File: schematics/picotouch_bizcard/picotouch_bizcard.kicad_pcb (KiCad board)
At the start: 2 copper layers, 88.9 x 50.8 mm, 48 parts, among them J2 AudioJack4, SW1 Capacitive Button, SW10 Capacitive Button, SW11 Capacitive Button, SW12 Capacitive Button, SW2 Capacitive Button, SW3 Capacitive Button, SW4 Capacitive Button, SW5 Capacitive Button, SW6 Capacitive Button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

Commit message: silkscreen
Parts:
- moved R16 1.02 mm to (132.1, 71.1)
- moved D6 0.89 mm to (127.0, 71.1)
- moved U1 0.51 mm to (127.8, 50.8)
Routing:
- net +3.3V: track 115.2 -> 114.1 mm
- net /TOUCH11: track 62.5 -> 63.2 mm
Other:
- board text added: "0"
- board text added: "1"
- board text added: "2"
- board text added: "3"
- board text added: "4"
- board text added: "5"
- board text added: "6"
- board text added: "7"
- board text added: "8"
- board text added: "<>"
- board text added: "@todbot"
- board text added: "MIDI OUT TRS-A"
- board text added: "X"
- board text added: "picotouch_bizcard 5 Jun 2024 - @todbot / Tod Kurt github.com/todbot/picotouch_bizcard"
- board text added: "picotouch_bizcard USB/MIDI controller"

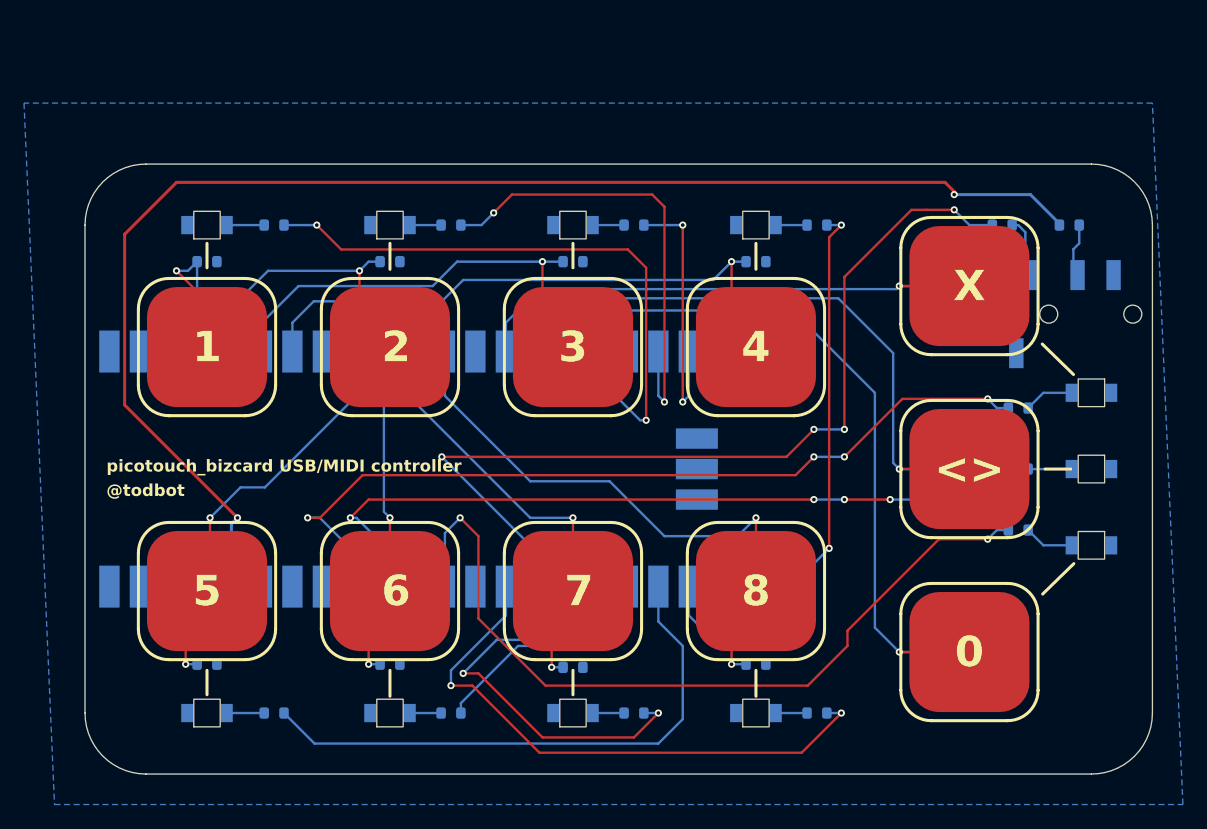
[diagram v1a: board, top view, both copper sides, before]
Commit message: added tx/rx test points and mounting hole
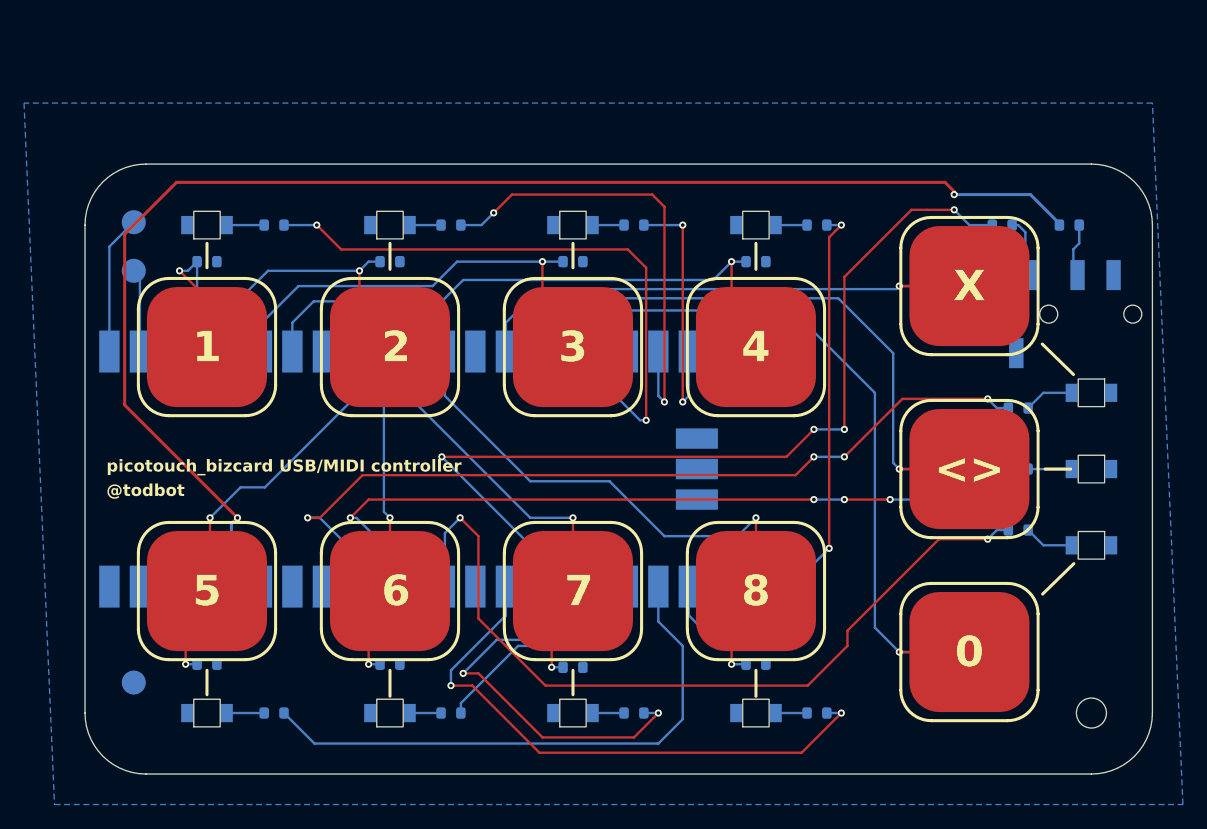
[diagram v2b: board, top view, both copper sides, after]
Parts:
- added H1: MountingHole, MountingHole:MountingHole_2.5mm, F.Cu at (185.4, 71.1)
- added TP1: TX, TestPoint:TestPoint_Pad_D2.0mm, B.Cu at (105.7, 30.2)
- added TP2: RX, TestPoint:TestPoint_Pad_D2.0mm, B.Cu at (105.7, 34.3)
- added TP3: GND, TestPoint:TestPoint_Pad_D2.0mm, B.Cu at (105.7, 68.6)
- SW1: footprint todbot_stuff:Pad-CapacitiveTouch-SparkFun -> SparkFun-Switch:Pad-CapacitiveTouch
- renumbered J2 to J1
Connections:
- U1 pad 1: unconnected-(U1-GPIO0-Pad1) -> /TX
- U1 pad 2: unconnected-(U1-GPIO1-Pad2) -> /RX
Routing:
- net /TX: track 0.00 -> 12.5 mm
- net /RX: track 0.00 -> 7.83 mm
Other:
- board text added: "gnd"
- board text added: "tx rx"

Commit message: submit to fab
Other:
- board text added: "JLCJLCJLCJLC"
- board text added: "picotouch_bizcard USB/MIDI controller / @todbot"
- board text removed: "@todbot"
- board text removed: "picotouch_bizcard USB/MIDI controller"
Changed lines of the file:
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@@
 		(sheetname "Root")
 		(sheetfile "picotouch_bizcard.kicad_sch")
-		(attr exclude_from_pos_files)
+		(attr exclude_from_pos_files exclude_from_bom)
 		(fp_circle
 			(center 0 0)
@@
 		(sheetname "Root")
 		(sheetfile "picotouch_bizcard.kicad_sch")
-		(attr exclude_from_pos_files)
+		(attr exclude_from_pos_files exclude_from_bom)
 		(fp_circle
 			(center 0 0)
@@
 		(sheetname "Root")
 		(sheetfile "picotouch_bizcard.kicad_sch")
-		(attr exclude_from_pos_files)
+		(attr exclude_from_pos_files exclude_from_bom)
 		(fp_circle
 			(center 0 0)
@@
 		(tags "3.5mm jack mic microphone phones headphones 4pins audio plug")
 		(property "Reference" "J1"
-			(at 0.05 5.35 180)
+			(at -1.33 -0.202 180)
 			(layer "B.SilkS")
 			(effects
@@
 		(layer "Edge.Cuts")
 	)
+	(gr_text "JLCJLCJLCJLC"
+		(at 183.515 71.12 0)
+		(layer "B.SilkS")
+		(effects
+			(font
+				(size 1.016 1.016)
+				(thickness 0.1)
+			)
+			(justify left mirror)
+		)
+	)
 	(gr_text "MIDI OUT\nTRS-A"
 		(at 177.165 40.005 0)
@@
 		)
 	)
-	(gr_text "@todbot\n"
-		(at 103.378 52.578 0)
-		(layer "F.SilkS")
-		(effects
-			(font
-				(size 1 1)
-				(thickness 0.2)
-				(bold yes)
-			)
-			(justify left)
-		)
-	)
 	(gr_text "0"
 		(at 175.26 66.04 0)
@@
 		)
 	)
-	(gr_text "picotouch_bizcard USB/MIDI controller"
+	(gr_text "picotouch_bizcard USB/MIDI controller / @todbot"
 		(at 103.378 50.546 0)
 		(layer "F.SilkS")
